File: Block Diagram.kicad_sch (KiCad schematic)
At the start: 0 parts

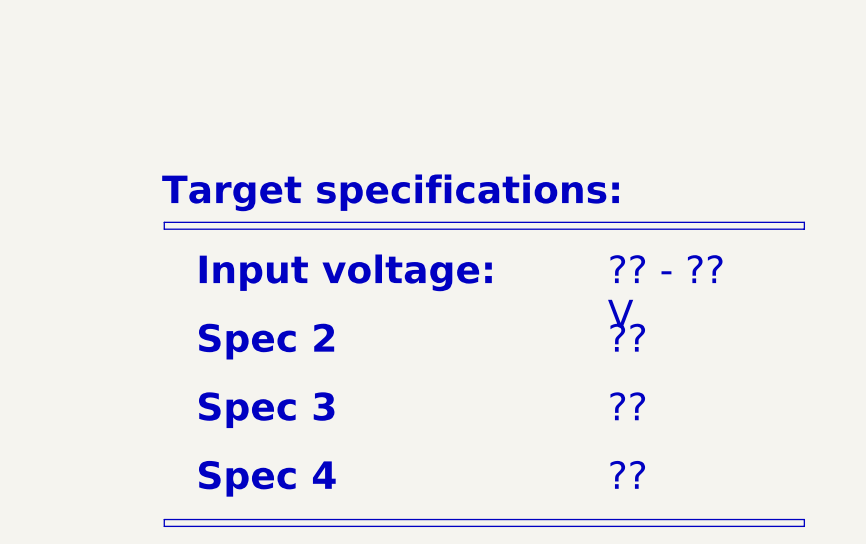
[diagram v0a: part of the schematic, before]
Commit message: New 3D path for trafo
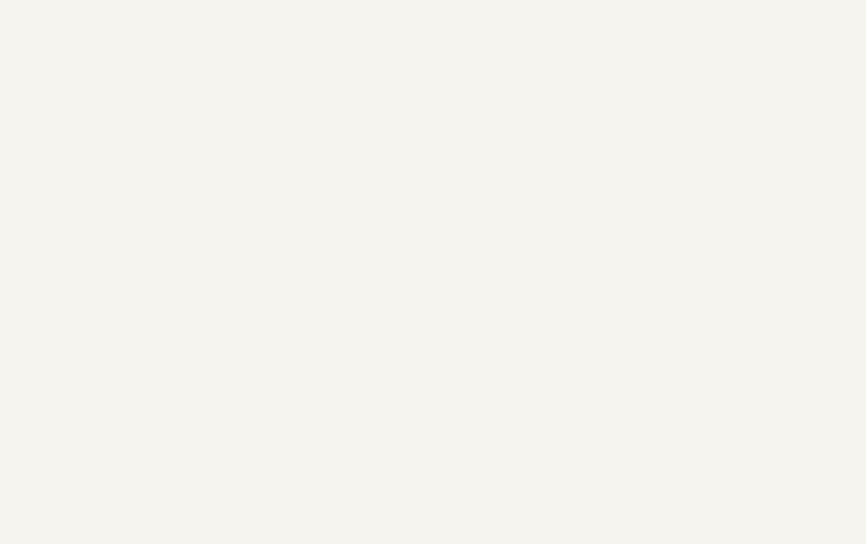
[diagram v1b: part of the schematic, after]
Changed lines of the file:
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@@
-	)
-	(rectangle
-		(start 328.422 234.95)
-		(end 399.542 235.712)
-		(stroke
-			(width 0)
-			(type default)
-			(color 0 0 0 1)
-		)
-		(fill
-			(type color)
-			(color 0 0 0 1)
-		)
 	)
 	(rectangle
@@
 	)
 	(rectangle
-		(start 328.422 201.93)
-		(end 399.542 202.692)
-		(stroke
-			(width 0)
-			(type default)
-			(color 0 0 0 1)
-		)
-		(fill
-			(type color)
-			(color 0 0 0 1)
-		)
-	)
-	(rectangle
 		(start 71.12 80.01)
 		(end 101.6 95.25)
@@
 		)
 	)
-	(text_box "Spec 4"
-		(exclude_from_sim no)
-		(at 329.692 226.06 0)
-		(size 44.45 7.62)
-		(margins 2.2859 2.2859 2.2859 2.2859)
-		(stroke
-			(width -0.0001)
-			(type default)
-		)
-		(fill
-			(type none)
-		)
-		(effects
-			(font
-				(face "Times New Roman")
-				(size 3.048 3.048)
-				(thickness 0.4572)
-				(bold yes)
-				(color 0 0 0 1)
-			)
-			(justify left top)
-		)
-	)
 	(text_box "BLOCK H"
 		(exclude_from_sim no)
@@
 		)
 	)
-	(text_box "?? - ?? V"
-		(exclude_from_sim no)
-		(at 375.412 203.2 0)
-		(size 24.13 7.62)
-		(margins 2.2859 2.2859 2.2859 2.2859)
-		(stroke
-			(width -0.0001)
-			(type default)
-		)
-		(fill
-			(type none)
-		)
-		(effects
-			(font
-				(face "Times New Roman")
-				(size 3.048 3.048)
-				(color 0 0 0 1)
-			)
-			(justify left top)
-		)
-	)
 	(text_box "Block\nDescription"
 		(exclude_from_sim no)
@@
 				(thickness 0.254)
 				(bold yes)
-				(color 0 0 0 1)
-			)
-			(justify left top)
-		)
-	)
-	(text_box "??"
-		(exclude_from_sim no)
-		(at 375.412 226.06 0)
-		(size 24.13 7.62)
-		(margins 2.2859 2.2859 2.2859 2.2859)
-		(stroke
-			(width -0.0001)
-			(type default)
-		)
-		(fill
-			(type none)
-		)
-		(effects
-			(font
-				(face "Times New Roman")
-				(size 3.048 3.048)
 				(color 0 0 0 1)
 			)
@@
 		)
 	)
-	(text_box "??"
-		(exclude_from_sim no)
-		(at 375.412 210.82 0)
-		(size 24.13 7.62)
-		(margins 2.2859 2.2859 2.2859 2.2859)
-		(stroke
-			(width -0.0001)
-			(type default)
-		)
-		(fill
-			(type none)
-		)
-		(effects
-			(font
-				(face "Times New Roman")
-				(size 3.048 3.048)
-				(color 0 0 0 1)
-			)
-			(justify left top)
-		)
-	)
-	(text_box "Input voltage:"
-		(exclude_from_sim no)
-		(at 329.692 203.2 0)
-		(size 41.91 7.62)
-		(margins 2.2859 2.2859 2.2859 2.2859)
-		(stroke
-			(width -0.0001)
-			(type default)
-		)
-		(fill
-			(type none)
-		)
-		(effects
-			(font
-				(face "Times New Roman")
-				(size 3.048 3.048)
-				(thickness 0.4572)
-				(bold yes)
-				(color 0 0 0 1)
-			)
-			(justify left top)
-		)
-	)
 	(text_box "SECTION"
 		(exclude_from_sim no)
@@
 		)
 	)
-	(text_box "Target specifications:"
-		(exclude_from_sim no)
-		(at 325.882 194.31 0)
-		(size 73.66 7.62)
-		(margins 2.2859 2.2859 2.2859 2.2859)
-		(stroke
-			(width -0.0001)
-			(type default)
-		)
-		(fill
-			(type none)
-		)
-		(effects
-			(font
-				(face "Times New Roman")
-				(size 3.048 3.048)
-				(thickness 0.4572)
-				(bold yes)
-				(color 0 0 0 1)
-			)
-			(justify left top)
-		)
-	)
 	(text_box "???"
 		(exclude_from_sim no)
@@
 		)
 	)
-	(text_box "Spec 3"
-		(exclude_from_sim no)
-		(at 329.692 218.44 0)
-		(size 41.91 7.62)
-		(margins 2.2859 2.2859 2.2859 2.2859)
-		(stroke
-			(width -0.0001)
-			(type default)
-		)
-		(fill
-			(type none)
-		)
-		(effects
-			(font
-				(face "Times New Roman")
-				(size 3.048 3.048)
-				(thickness 0.4572)
-				(bold yes)
-				(color 0 0 0 1)
-			)
-			(justify left top)
-		)
-	)
-	(text_box "??"
-		(exclude_from_sim no)
-		(at 375.412 218.44 0)
-		(size 24.13 7.62)
-		(margins 2.2859 2.2859 2.2859 2.2859)
-		(stroke
-			(width -0.0001)
-			(type default)
-		)
-		(fill
-			(type none)
-		)
-		(effects
-			(font
-				(face "Times New Roman")
-				(size 3.048 3.048)
-				(color 0 0 0 1)
-			)
-			(justify left top)
-		)
-	)
-	(text_box "Spec 2"
-		(exclude_from_sim no)
-		(at 329.692 210.82 0)
-		(size 43.18 7.62)
-		(margins 2.2859 2.2859 2.2859 2.2859)
-		(stroke
-			(width -0.0001)
-			(type default)
-		)
-		(fill
-			(type none)
-		)
-		(effects
-			(font
-				(face "Times New Roman")
-				(size 3.048 3.048)
-				(thickness 0.4572)
-				(bold yes)
-				(color 0 0 0 1)
-			)
-			(justify left top)
-		)
-	)

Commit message: testing lib issue
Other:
- added sheet Schematic (Schematic.kicad_sch)
- note added: "1 2 3 4"
- note added: "AliExpress module"
- note added: "Page 3"
- note added: "Vout+ Vout- Vin+ Vin-"
- note removed: "+??V"
- note removed: "+A3V3"

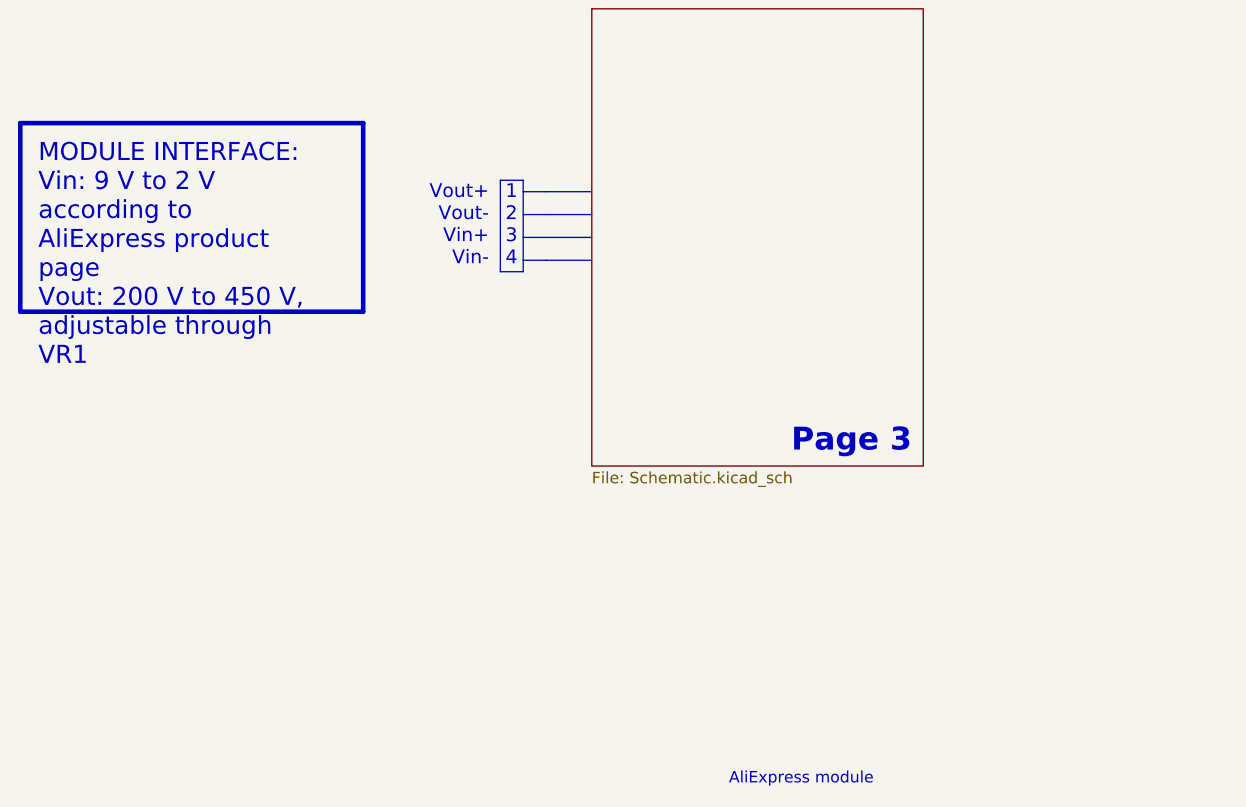
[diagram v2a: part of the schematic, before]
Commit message: General notes added
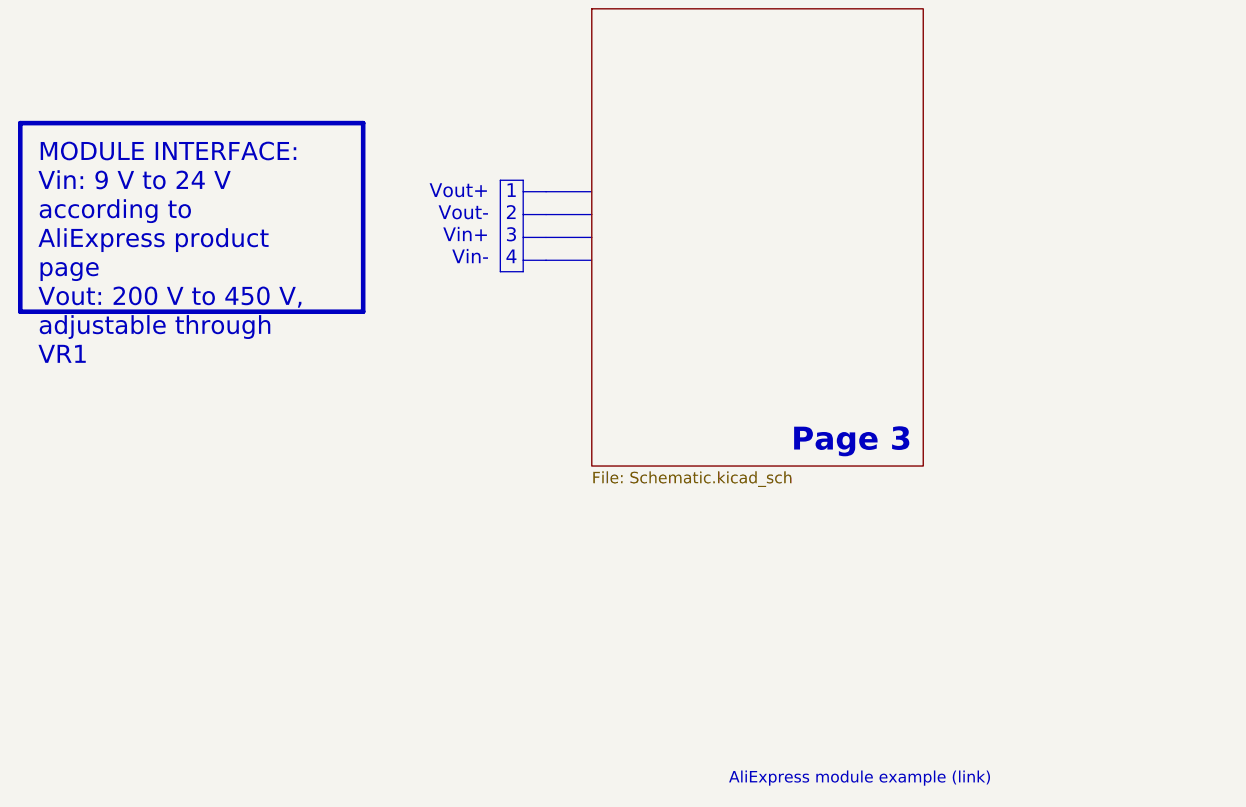
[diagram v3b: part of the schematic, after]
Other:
- note added: "AliExpress module example (link)"
- note removed: "AliExpress module"
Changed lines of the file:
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@@
 	(title_block
 		(title "Block Diagram")
-		(date "2025-01-12")
+		(date "2025-12-20")
 		(rev "${REVISION}")
 		(company "${COMPANY}")
@@
 		)
 	)
-	(text "AliExpress module"
+	(text "AliExpress module example (link)"
 		(exclude_from_sim no)
 		(at 142.24 162.56 0)
@@
 		)
 	)
-	(text_box "MODULE INTERFACE:\nVin: 9 V to 2 V according to AliExpress product page\nVout: 200 V to 450 V, adjustable through VR1"
+	(text_box "MODULE INTERFACE:\nVin: 9 V to 24 V according to AliExpress product page\nVout: 200 V to 450 V, adjustable through VR1"
 		(exclude_from_sim no)
 		(at 63.5 88.9 0)
